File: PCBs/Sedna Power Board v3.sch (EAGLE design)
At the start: 21 parts

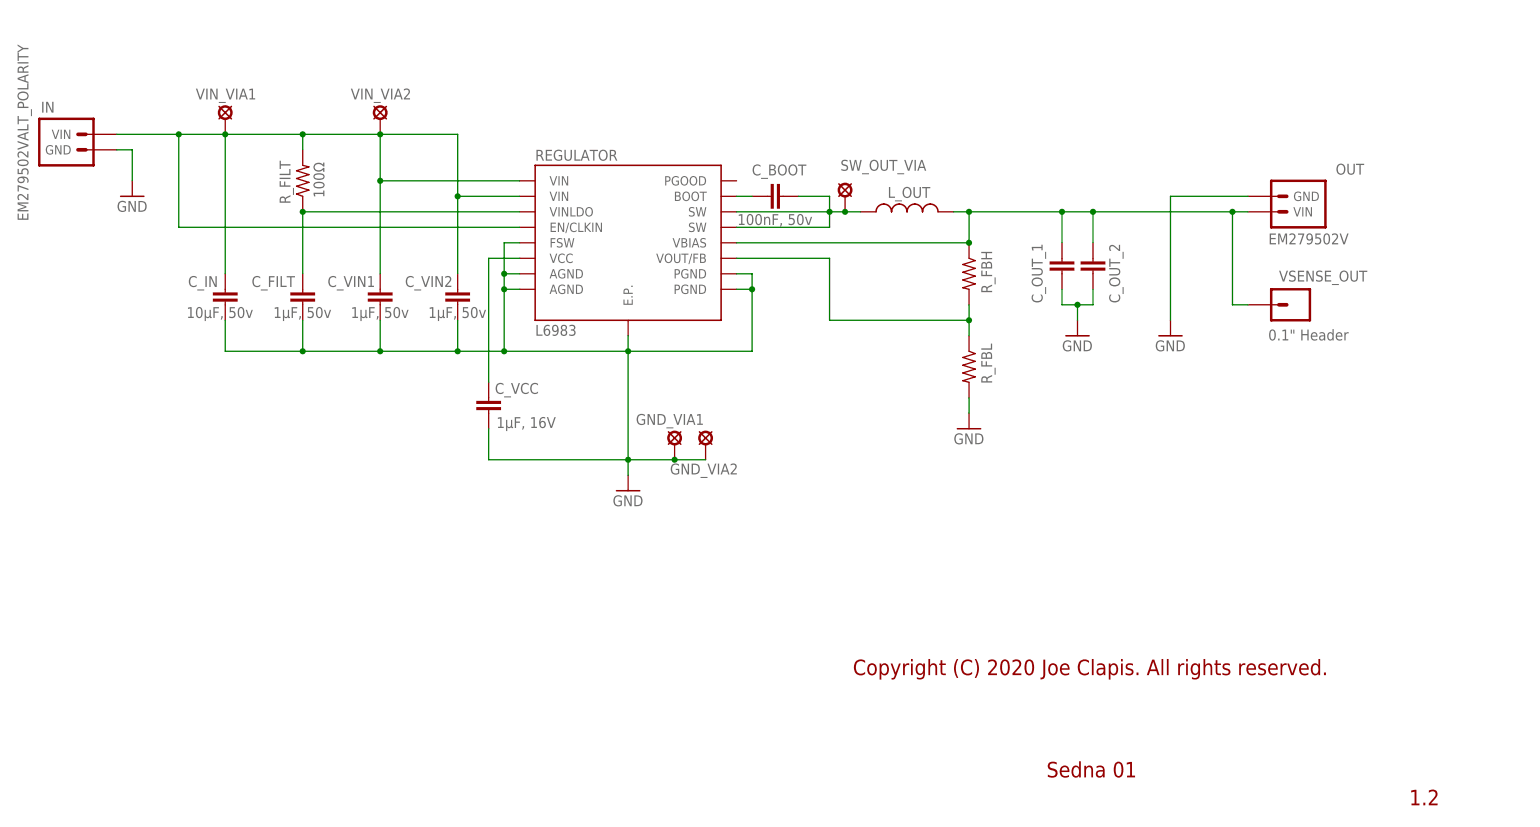
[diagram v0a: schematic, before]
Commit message: v3 of the power board, now with a trimpot on the FB voltage divider for output voltage adjustments.
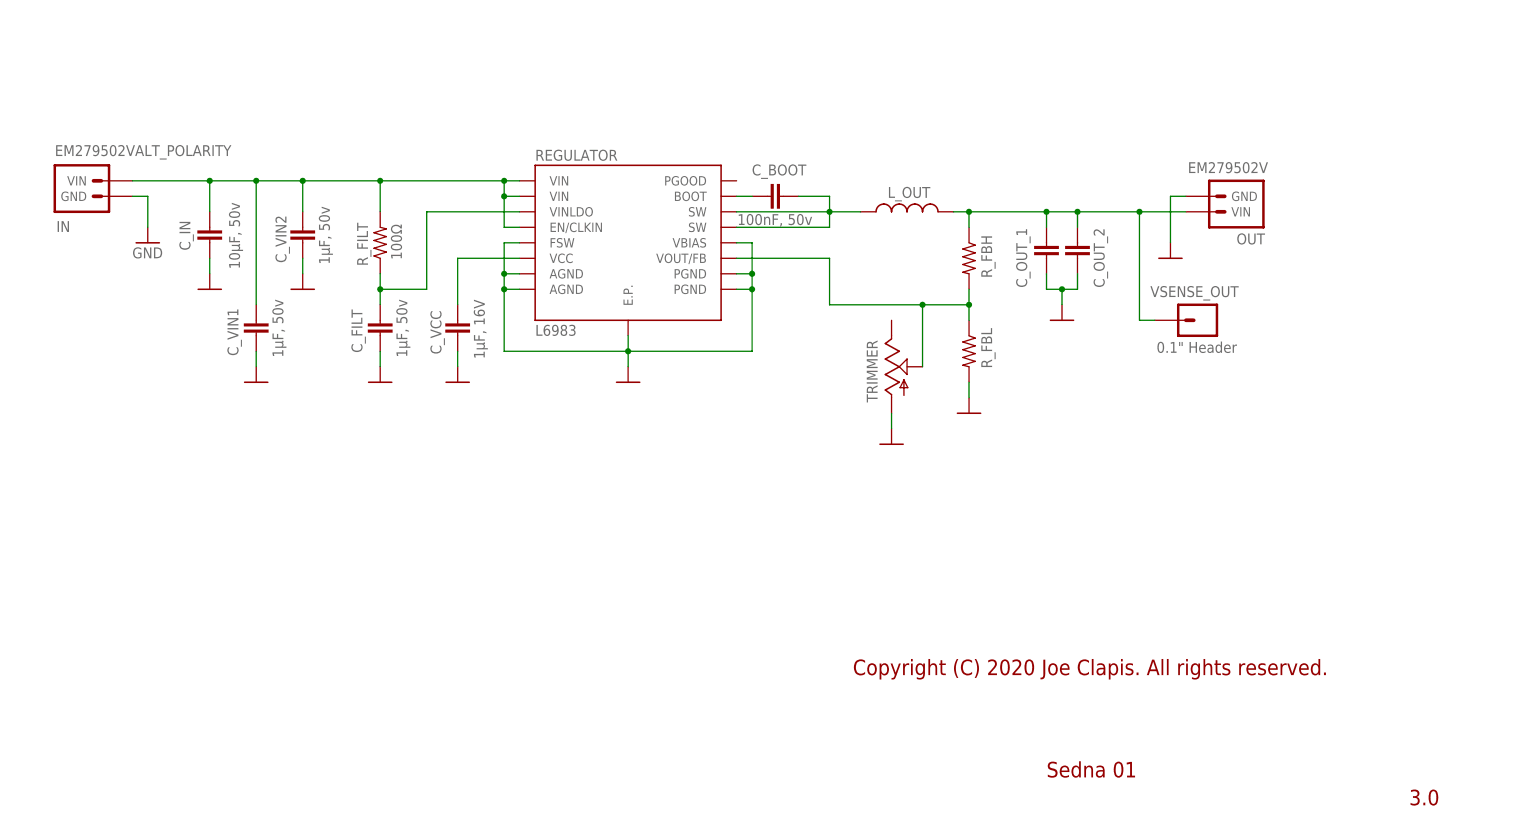
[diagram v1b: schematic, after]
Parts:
- removed GND_VIA1, GND_VIA2, SW_OUT_VIA, VIN_VIA1, VIN_VIA2: LSP13, solpad:LSP13
- added TRIMMER: (no value), Sedna Components:BOURNS_3361S
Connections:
- net FB: now also TRIMMER.S
- net GND: now also REGULATOR.VBIAS, TRIMMER.A; no longer GND_VIA1.MP, GND_VIA2.MP
- net SW_OUT: no longer SW_OUT_VIA.MP
- net V_IN: no longer VIN_VIA1.MP, VIN_VIA2.MP
- net V_OUT: no longer REGULATOR.VBIAS
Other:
- note added: "3.0"
- note removed: "1.2"
- moved on the sheet: C_FILT, C_IN, C_OUT_1, C_OUT_2, C_VCC, C_VIN1, C_VIN2, IN, OUT, R_FBH, R_FBL, R_FILT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
